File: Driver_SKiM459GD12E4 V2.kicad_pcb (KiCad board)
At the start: 4 copper layers, 169.2 x 116 mm, 340 parts, among them J1 2-338069-0, J13 EL1, J14 GL1, J15 NTC1_A, J16 NTC1_B, J17 GH1, J18 OUT1, J19 CH1, J20 EL2, J21 GL2, J22 NTC2_A, J23 NTC2_B, J24 GH2, J25 OUT2, J26 CH2, J27 EL3, J28 GL3, J29 NTC3_A, J30 NTC3_B, J31 GH3, J32 OUT3, J33 CH3, Q1 MJD44H11T4G, Q10 MJD45H11T4G, Q11 MJD44H11T4G, Q12 MJD45H11T4G, Q2 MJD45H11T4G, Q3 MJD44H11T4G, Q4 MJD45H11T4G, Q5 MJD44H11T4G, Q6 MJD45H11T4G, Q7 MJD44H11T4G, Q8 MJD45H11T4G, Q9 MJD44H11T4G, U1 LM2904, U2 R-785.0-1.0, U3 LM397, U4 HCPL-0611

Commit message: Нашёл ошибки
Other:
- board text added: "1. Инвертировать ШИМ"
- board text added: "2. Исправить отверстия под крепления"
- board text added: "3. Инвертировать логику PTC"
- board text added: "4. Заменить R141 на 1,5кОм"
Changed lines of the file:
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@@
     (fp_line (start -0.227064 -0.735) (end 0.227064 -0.735) (layer "B.SilkS") (width 0.12))
     (fp_line (start -0.227064 0.735) (end 0.227064 0.735) (layer "B.SilkS") (width 0.12))
-    (fp_line (start -1.85 0.95) (end 1.85 0.95) (layer "B.CrtYd") (width 0.05))
     (fp_line (start 1.85 -0.95) (end -1.85 -0.95) (layer "B.CrtYd") (width 0.05))
+    (fp_line (start -1.85 0.95) (end 1.85 0.95) (layer "B.CrtYd") (width 0.05))
     (fp_line (start 1.85 0.95) (end 1.85 -0.95) (layer "B.CrtYd") (width 0.05))
     (fp_line (start -1.85 -0.95) (end -1.85 0.95) (layer "B.CrtYd") (width 0.05))
-    (fp_line (start -1 0.625) (end 1 0.625) (layer "B.Fab") (width 0.1))
-    (fp_line (start 1 -0.625) (end -1 -0.625) (layer "B.Fab") (width 0.1))
     (fp_line (start -1 -0.625) (end -1 0.625) (layer "B.Fab") (width 0.1))
+    (fp_line (start -1 0.625) (end 1 0.625) (layer "B.Fab") (width 0.1))
     (fp_line (start 1 0.625) (end 1 -0.625) (layer "B.Fab") (width 0.1))
+    (fp_line (start 1 -0.625) (end -1 -0.625) (layer "B.Fab") (width 0.1))
     (pad "1" smd roundrect (at -1 0 270) (size 1.2 1.4) (layers "B.Cu" "B.Paste" "B.Mask") (roundrect_rratio 0.208333)
       (net 166 "Net-(R101-Pad2)") (pintype "passive"))
@@
   )
   (gr_text "Driver SKiM459GD12E4 V2" (at 93.472 37.592) (layer "F.SilkS")
-    (effects (font (size 2 2) (thickness 0.4) italic))
+    (effects (font (size 2 2) (thickness 0.4)))
+  )
+  (gr_text "3. Инвертировать логику PTC" (at 95.25 176.725) (layer "User.1")
+    (effects (font (size 3 3) (thickness 0.45)))
+  )
+  (gr_text "1. Инвертировать ШИМ" (at 87.63 164.5) (layer "User.1")
+    (effects (font (size 3 3) (thickness 0.45)))
+  )
+  (gr_text "2. Исправить отверстия под крепления " (at 107.95 170.6) (layer "User.1")
+    (effects (font (size 3 3) (thickness 0.45)))
+  )
+  (gr_text "4. Заменить R141 на 1,5кОм" (at 95.25 182.88) (layer "User.1")
+    (effects (font (size 3 3) (thickness 0.45)))
   )
   (segment (start 107.9285 120.142) (end 107.9285 117.8935) (width 0.5) (layer "F.Cu") (net 1))
@@
   (segment (start 200.406 81.216) (end 201.74 82.55) (width 1) (layer "F.Cu") (net 19))
   (via (at 201.74 82.55) (size 0.8) (drill 0.4) (layers "F.Cu" "B.Cu") (net 19))
-  (segment (start 202.502 81.788) (end 201.74 82.55) (width 1) (layer "B.Cu") (net 19))
   (segment (start 205.46 81.788) (end 202.502 81.788) (width 1) (layer "B.Cu") (net 19))
+  (segment (start 202.502 81.788) (end 201.74 82.55) (width 1) (layer "B.Cu") (net 19))
   (segment (start 206.912 87.722) (end 201.74 82.55) (width 1) (layer "B.Cu") (net 19))
   (segment (start 210.309 60.325) (end 206.912 63.722) (width 0.5) (layer "B.Cu") (net 20))

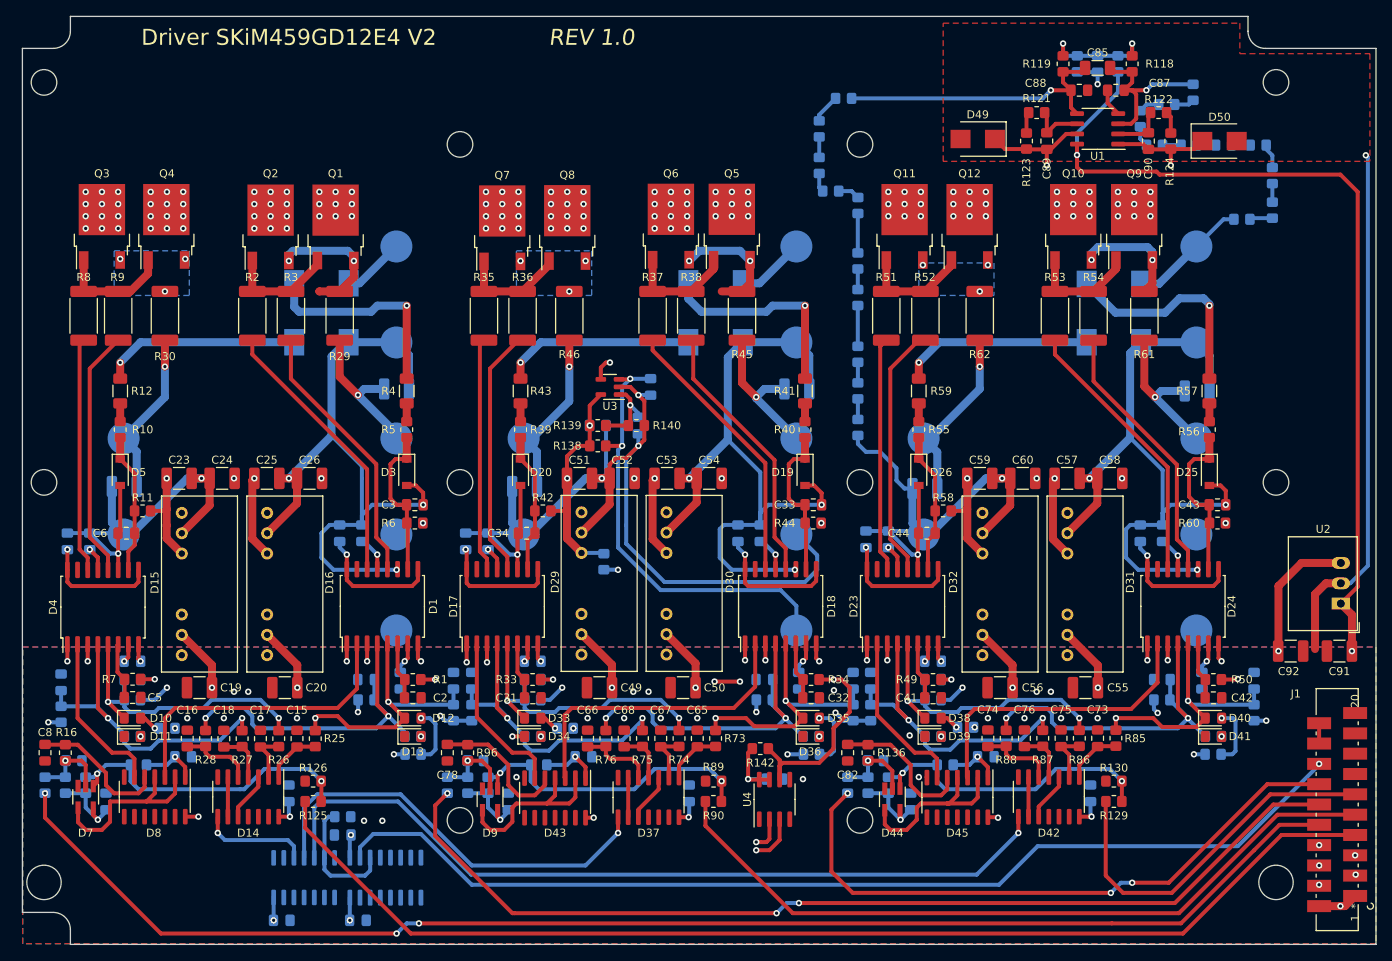
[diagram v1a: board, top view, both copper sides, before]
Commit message: Исправил ошибки, добавил резисторы в затвор, ревизия 2.0
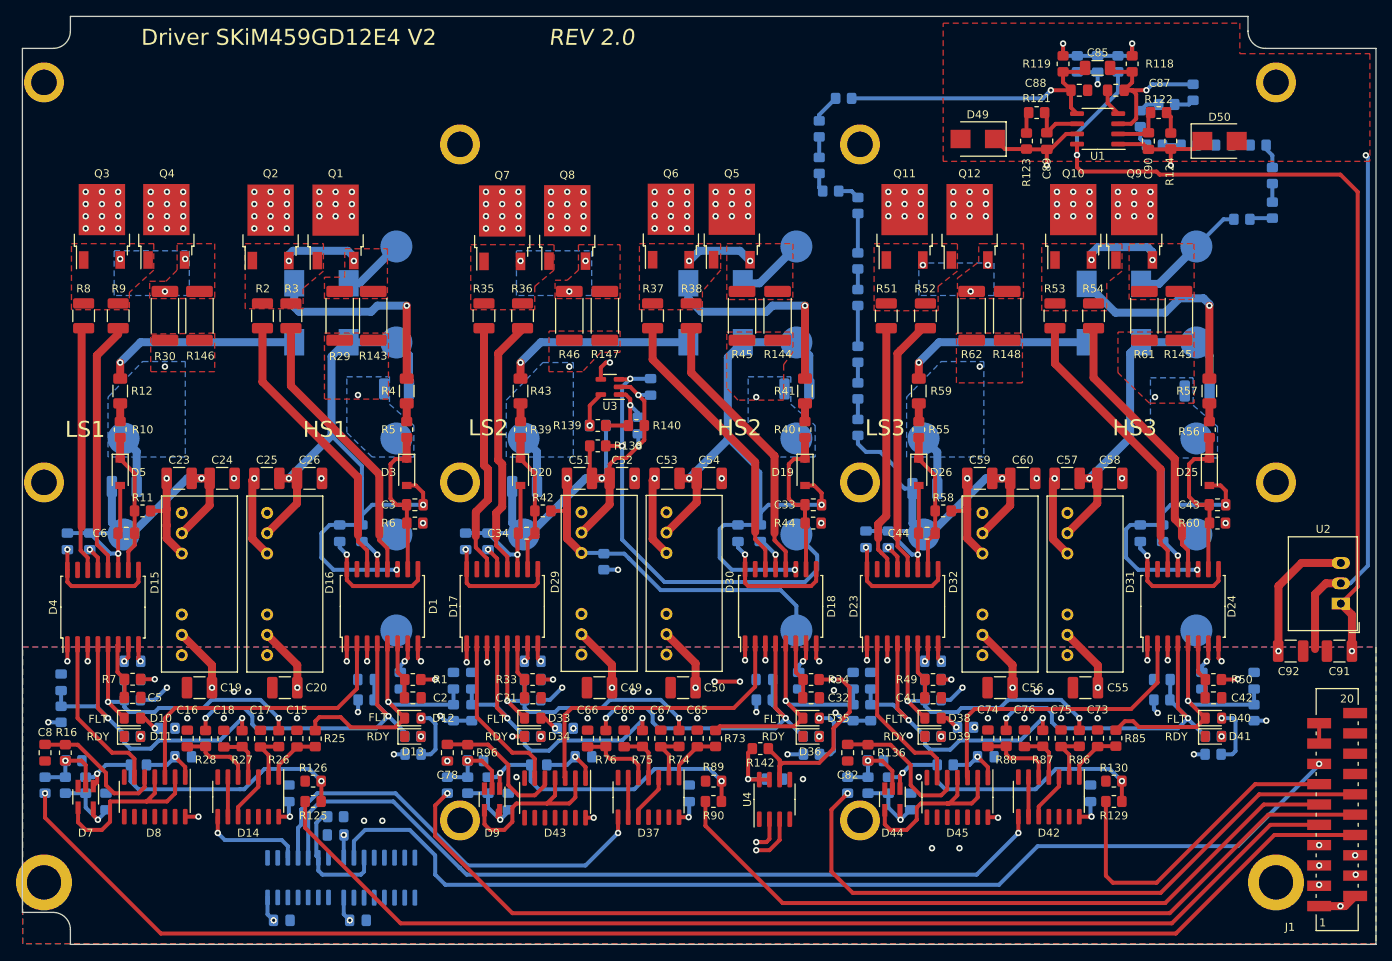
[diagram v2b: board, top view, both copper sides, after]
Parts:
- added R143: 3.9, Resistor_SMD:R_2512_6332Metric_Pad1.40x3.35mm_HandSolder, F.Cu at (104.0, 72.4)
- added R144: 3.9, Resistor_SMD:R_2512_6332Metric_Pad1.40x3.35mm_HandSolder, F.Cu at (154.6, 72.4)
- added R145: 3.9, Resistor_SMD:R_2512_6332Metric_Pad1.40x3.35mm_HandSolder, F.Cu at (204.7, 72.4)
- added R146: 3.9, Resistor_SMD:R_2512_6332Metric_Pad1.40x3.35mm_HandSolder, F.Cu at (82.3, 72.4)
- added R147: 3.9, Resistor_SMD:R_2512_6332Metric_Pad1.40x3.35mm_HandSolder, F.Cu at (133.0, 72.4)
- added R148: 3.9, Resistor_SMD:R_2512_6332Metric_Pad1.40x3.35mm_HandSolder, F.Cu at (183.3, 72.4)
- H1, H10, H2, H3, H4, H5, H6, H7, H8, H9: footprint MountingHole:MountingHole_3.2mm_M3 -> Mounting_Hole_My:M3
- H11, H12: footprint MountingHole:MountingHole_4.3mm_M4 -> Mounting_Hole_My:M4
- R139: value 1k -> 1.8k
- R140: value 1.8k -> 1k
- R141: value 300 -> 1.5k
- R2, R3, R35, R36, R37, R38, R51, R52, R53, R54, R8, R9: footprint Resistor_SMD:R_2512_6332Metric_Pad1.40x3.35mm_HandSolder -> Resistor_SMD:R_1210_3225Metric_Pad1.30x2.65mm_HandSolder
- moved R2 1.27 mm to (90.2, 72.4)
- moved R62 1.02 mm to (178.8, 72.4)
- moved C93 0.89 mm to (99.3, 137.3)
- moved R137 0.89 mm to (99.3, 135.0)
- moved D51 0.76 mm to (94.6, 142.6)
- moved D52 0.76 mm to (104.8, 142.6)
- moved D9 0.25 mm to (118.9, 132.8)
- turned R138 to 0 degrees
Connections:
- net NTC1_A renamed PTC1_A
- net NTC1_B renamed PTC1_B
- net NTC3_A renamed PTC3_A
- net NTC3_B renamed PTC3_B
- C98 pad 1: NTC2_A -> PTC2_B
- J22 pad 1: NTC2_A -> +15V_L2
- J23 pad 1: EL2 -> PTC2_B
- R125 pad 1: HB1_TOP -> HB1_BOT
- R127 pad 1: HB1_BOT -> HB1_TOP
- R129 pad 1: HB3_TOP -> HB3_BOT
- R131 pad 1: HB3_BOT -> HB3_TOP
- R138 pad 1: NTC2_A -> EL2
- R138 pad 2: +15V_L2 -> PTC2_B
- R89 pad 1: HB2_TOP -> HB2_BOT
- R91 pad 1: HB2_BOT -> HB2_TOP
- U3 pad 3: NTC2_A -> PTC2_B
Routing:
- net PTC2_B: track 0.00 -> 59.3 mm, vias 0 -> 2
- net NTC2_A: track 56.1 -> 0.00 mm, vias 2 -> 0
- net EL2: track 124.5 -> 82.3 mm
- net HB2_BOT: track 126.1 -> 88.9 mm, vias 3 -> 0
- net HB3_BOT: track 78.3 -> 41.4 mm, vias 3 -> 0
- net HB2_TOP: track 93.9 -> 130.1 mm, vias 0 -> 1
- net HB3_TOP: track 46.5 -> 82.3 mm, vias 0 -> 1
- net HB1_BOT: track 173.9 -> 140.1 mm, vias 3 -> 0
- net HB1_TOP: track 145.1 -> 177.9 mm, vias 0 -> 1
- net +15V_L2: track 31.1 -> 52.2 mm
- net GH2: track 19.1 -> 0.00 mm
- net GH3: track 19.0 -> 0.00 mm
- net GH1: track 18.8 -> 0.65 mm
- net GL3: track 22.6 -> 6.97 mm
- net BL1_CLOSE: track 14.6 -> 0.00 mm
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- added copper zone on F.Cu, net BH1_CLOSE
- added copper zone on F.Cu, net BH2_CLOSE
- added copper zone on F.Cu, net BH3_CLOSE
- added copper zone on F.Cu, net BL1_CLOSE
- added copper zone on F.Cu, net BL2_CLOSE
- added copper zone on F.Cu, net BL3_CLOSE
- added copper zone on B.Cu, net GH1
- added copper zone on F.Cu, net GH1
- added copper zone on B.Cu, net GH2
- added copper zone on F.Cu, net GH2
- added copper zone on B.Cu, net GH3
- added copper zone on F.Cu, net GH3
- added copper zone on B.Cu, net GL1
- added copper zone on F.Cu, net GL1
- added copper zone on B.Cu, net GL2
- added copper zone on F.Cu, net GL2
- added copper zone on B.Cu, net GL3
- added copper zone on F.Cu, net GL3
- added copper zone on F.Cu, net Net-(Q1-Pad3)
- added copper zone on F.Cu, net Net-(Q10-Pad3)
- added copper zone on F.Cu, net Net-(Q11-Pad3)
- added copper zone on F.Cu, net Net-(Q3-Pad3)
- added copper zone on F.Cu, net Net-(Q5-Pad3)
- added copper zone on F.Cu, net Net-(Q7-Pad3)
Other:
- board text added: "FLT"
- board text added: "HS1"
- board text added: "HS2"
- board text added: "HS3"
- board text added: "LS1"
- board text added: "LS2"
- board text added: "LS3"
- board text added: "RDY"
- board text added: "REV 2.0"
- board text removed: "1. Инвертировать ШИМ"
- board text removed: "2. Исправить отверстия под крепления"
- board text removed: "3. Инвертировать логику PTC"
- board text removed: "4. Заменить R141 на 1,5кОм"
- board text removed: "REV 1.0"

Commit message: REV2.1 - добавил конденсатор по питанию измерения DC
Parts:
- added C99: 0.1u, Capacitor_SMD:C_0805_2012Metric_Pad1.18x1.45mm_HandSolder, B.Cu at (194.5, 48.5)
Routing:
- net GND: track 189.2 -> 193.3 mm
- net +15V: track 167.9 -> 169.8 mm
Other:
- board text added: "REV 2.1"
- board text removed: "REV 2.0"
